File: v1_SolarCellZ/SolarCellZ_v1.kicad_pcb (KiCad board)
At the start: 6 copper layers, 48.4 x 48.4 mm, 22 parts, among them J1 XF2M-1015-1A, Q1 IRLML2803, U1 NDS8434

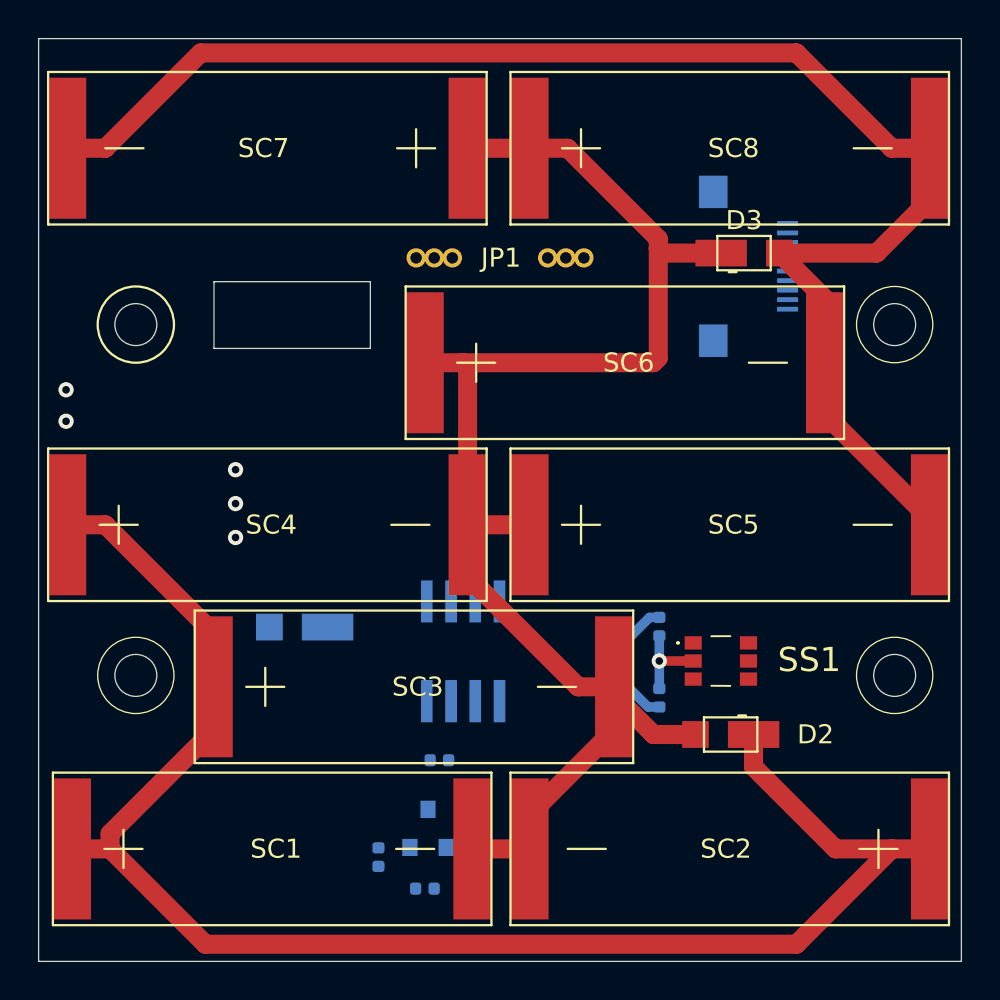
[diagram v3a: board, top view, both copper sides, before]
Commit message: X and Z panels are ready
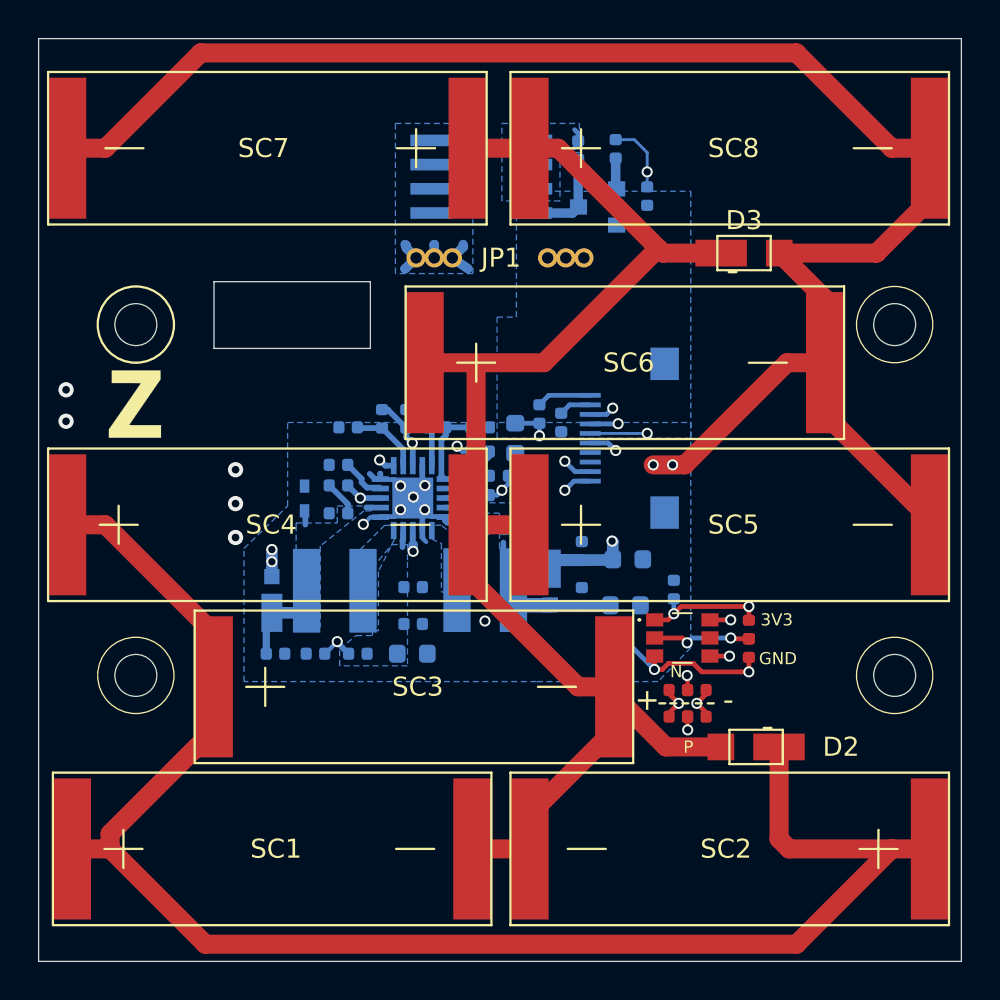
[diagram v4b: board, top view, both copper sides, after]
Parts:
- removed the C1 at (120.1, 72.7)
- removed the R1 at (122.6, 70.8)
- removed the R2 at (122.6, 74.6)
- removed the R3 at (107.8, 82.9)
- removed the R4 at (110.3, 84.6)
- removed the R5 at (111.0, 77.9)
- added C1: 0.1uF, Capacitor_SMD:C_0402_1005Metric, B.Cu at (123.3, 68.9)
- added C1: 1.0uF, Capacitor_SMD:C_0402_1005Metric, B.Cu at (115.1, 62.9)
- added C10: 0.1uF, Capacitor_SMD:C_0402_1005Metric, B.Cu at (118.5, 69.3)
- added C11: 100uF, Capacitor_SMD:C_0603_1608Metric, B.Cu at (109.6, 72.3)
- added C12: 100uF, Capacitor_SMD:C_0603_1608Metric, B.Cu at (120.8, 69.7)
- added C13: 0.1uF, Capacitor_SMD:C_0402_1005Metric, B.Cu at (118.5, 66.9)
- added C14: 100uF, Capacitor_SMD:C_0603_1608Metric, B.Cu at (120.9, 67.3)
- added C2: 0.1uF, Capacitor_SMD:C_0402_1005Metric, B.Cu at (102.4, 72.3)
- added C3: 4.7uF, Capacitor_SMD:C_0402_1005Metric, B.Cu at (105.7, 64.9)
- added C4: 10nF, Capacitor_SMD:C_0402_1005Metric, B.Cu at (105.7, 62.4)
- added C6: 100uF, Capacitor_SMD:C_0603_1608Metric, B.Cu at (115.0, 61.0)
- added C7: 22uF, Capacitor_SMD:C_0402_1005Metric, B.Cu at (113.9, 65.7)
- added C8: 4.7uF, Capacitor_SMD:C_0402_1005Metric, B.Cu at (109.6, 68.8)
- added C9: 0.1uF, Capacitor_SMD:C_0402_1005Metric, B.Cu at (109.6, 70.7)
- added D2: MSS1P4-M3_89A, custom-footprints:MICROSMP, B.Cu at (116.8, 68.5)
- added D3: MSS1P4-M3_89A, custom-footprints:MICROSMP, B.Cu at (102.2, 69.5)
- added L1: 22uH-LPS4018-223MR, misc-circuits:LPS4018, B.Cu at (105.5, 69.0)
- added L2: 10uH-LPS4018-103MR, misc-circuits:LPS4018, B.Cu at (113.4, 68.9)
- added R1: 0, Resistor_SMD:R_0402_1005Metric, F.Cu at (127.3, 71.0)
- added R1: 0, Resistor_SMD:R_0402_1005Metric, B.Cu at (113.2, 63.9)
- added R10: 8.25M, Resistor_SMD:R_0402_1005Metric, B.Cu at (113.2, 61.7)
- added R11: 4.75M, Resistor_SMD:R_0402_1005Metric, B.Cu at (113.2, 62.9)
- added R14: 0, Resistor_SMD:R_0402_1005Metric, B.Cu at (105.7, 63.4)
- added R15: 0, Resistor_SMD:R_0402_1005Metric, B.Cu at (104.5, 72.3)
- added R16: 0, Resistor_SMD:R_0402_1005Metric, B.Cu at (106.7, 72.3)
- added R17: 0, Resistor_SMD:R_0402_1005Metric, B.Cu at (116.3, 59.7)
- added R18: 0, Resistor_SMD:R_0402_1005Metric, B.Cu at (117.4, 60.1)
- added R19: 0, Resistor_SMD:R_0402_1005Metric, F.Cu at (124.5, 74.2)
- added R2: 0, Resistor_SMD:R_0402_1005Metric, F.Cu at (123.6, 75.6)
- added R2: 0, Resistor_SMD:R_0402_1005Metric, F.Cu at (127.3, 72.0)
- added R3: 10k, Resistor_SMD:R_0402_1005Metric, B.Cu at (121.9, 48.3)
- added R3: 0, Resistor_SMD:R_0402_1005Metric, F.Cu at (124.5, 75.6)
- added R4: 4.7k, Resistor_SMD:R_0402_1005Metric, B.Cu at (120.3, 45.8)
- added R4: 0, Resistor_SMD:R_0402_1005Metric, F.Cu at (123.6, 74.2)
- added R5: 100k, Resistor_SMD:R_0402_1005Metric, B.Cu at (118.3, 45.8)
- added R5: 7.32M, Resistor_SMD:R_0402_1005Metric, B.Cu at (108.0, 59.9)
- added R6: 5.62M, Resistor_SMD:R_0402_1005Metric, B.Cu at (106.2, 60.4)
- added R7: 374K, Resistor_SMD:R_0402_1005Metric, B.Cu at (109.3, 59.9)
- added R8: 8.25M, Resistor_SMD:R_0402_1005Metric, B.Cu at (110.9, 60.4)
- added R9: 4.53M, Resistor_SMD:R_0402_1005Metric, B.Cu at (113.2, 60.4)
- added Ref**: Val**, custom-footprints:zpanel, F.Cu at (113.0, 59.4)
- added U2: Value, misc-circuits:QFN50P350X350X100-21N-D, B.Cu at (109.6, 64.1)
- D1: value SBDiode -> SDM20U40-7; footprint SolarCellParts:SB Diode -> misc-circuits:SOD523
- J1: footprint misc-circuits:XF2M-1015-1A -> custom-footprints:XF2M-1015-1A
- U1: footprint misc-circuits:NDS8434 -> custom-footprints:NDS8434
- moved Q1 33.8 mm to (119.3, 48.8), turned to 180 degrees
- moved U1 24.9 mm to (113.2, 47.2), turned to 270 degrees
- moved J1 13.7 mm to (118.9, 61.0), turned to 270 degrees
- moved D1 6.70 mm to (103.9, 64.2), turned to 90 degrees
- moved IC1 2.35 mm to (123.8, 71.4)
- moved D2 1.49 mm to (127.6, 77.2)
- renumbered SS1 to IC1
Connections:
- D2 pad 1: Net-(D1-Pad2) -> VSOLAR
- J1 pad 1: SDA1 -> BATT_P
- J1 pad 10: GND -> COIL_P
- J1 pad 2: BATT_P -> BATT_N
- J1 pad 3: SCL1 -> SDA1
- J1 pad 4: BATT_N -> SCL1
- J1 pad 6: COIL_N -> +3V3
- J1 pad 7: +3V3 -> GND
- J1 pad 8: COIL_N -> GND
- J1 pad 9: GND -> COIL_N
- JP1 pad 10: (no net) -> /VBURN
- JP1 pad 100: (no net) -> /VBURN
- JP1 pad 20: (no net) -> GND
- JP1 pad 200: (no net) -> GND
- SC1 pad 1: Net-(D1-Pad2) -> VSOLAR
- SC2 pad 1: Net-(D1-Pad2) -> VSOLAR
- SC3 pad 1: Net-(D1-Pad2) -> VSOLAR
- SC4 pad 1: Net-(D1-Pad2) -> VSOLAR
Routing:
- net /coil: track 0.00 -> 17213.2 mm, vias 0 -> 7
- net (no net): track 17144.3 -> 0.00 mm, vias 5 -> 0
- net VSOLAR: track 0.00 -> 92.9 mm
- net Net-(D1-Pad2): track 85.8 -> 0.00 mm
- net GND: track 90.1 -> 119.6 mm, vias 0 -> 11
- net COIL_P: track 0.00 -> 21.0 mm, vias 0 -> 2
- net BURN1: track 0.00 -> 20.4 mm, vias 0 -> 2
- net +3V3: track 3.20 -> 22.7 mm, vias 0 -> 4
- net SCL1: track 0.00 -> 17.1 mm, vias 0 -> 2
- net COIL_N: track 0.00 -> 16.6 mm, vias 0 -> 2
- net SDA1: track 0.00 -> 16.3 mm, vias 0 -> 2
- net /VBAT: track 0.00 -> 13.9 mm, vias 0 -> 2
- net Net-(R14-Pad1): track 0.00 -> 11.8 mm, vias 0 -> 2
- net VOUT_EN: track 0.00 -> 9.60 mm, vias 0 -> 2
- net Net-(C10-Pad1): track 0.00 -> 9.20 mm
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- added copper zone on B.Cu, net /VBURN
- added copper zone on B.Cu, net BATT_P
- added copper zone on B.Cu, net GND
- added copper zone on In3.Cu, net GND
- added copper zone on B.Cu, net Net-(C10-Pad1)
- added copper zone on B.Cu, net Net-(C11-Pad1)
- added copper zone on B.Cu, net Net-(L1-Pad2)
- added copper zone on B.Cu, net Net-(L2-Pad1)
- added copper zone on B.Cu, net VSOLAR
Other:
- net class Default: clearance 0.2 -> 0.127; trace_width 0.25 -> 0.2286; via_dia 0.8 -> 0.5842; via_drill 0.4 -> 0.381
- rule pad_to_mask_clearance: 0.051 -> 0.0508
- rule trace_clearance: 0.2 -> 0.127
- rule trace_min: 0.2 -> 0.1524
- rule via_min_size: 0.4 -> 0.45
- board text added: "+"
- board text added: "-"
- board text added: "3V3"
- board text added: "GND"
- board text added: "N"
- board text added: "P"
- board text added: "v00"
